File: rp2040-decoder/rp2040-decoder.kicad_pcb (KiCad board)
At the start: 4 copper layers, 19.6 x 8.6 mm, 57 parts, among them J4 5052702412, Q1 TPM2008, Q2 TPM2008, Q3 TPM2008, Q4 TPM2008, Q5 TPM2008, Q6 TPM2008, Q7 TPM2008, U1 W25Q64JVXGIQ, U2 AP63203WU, U3 RP2040, U4 MD9927, U5 MAX98357A, U6 LMV331, Y1 X252012MMB4SI

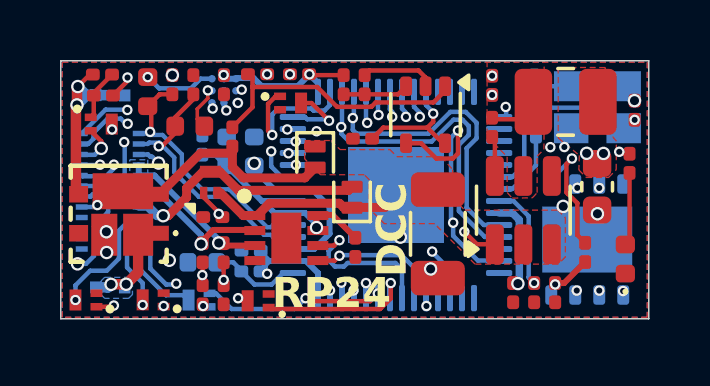
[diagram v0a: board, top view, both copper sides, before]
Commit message: fix: convert 0.2mm vias to 0.3mm
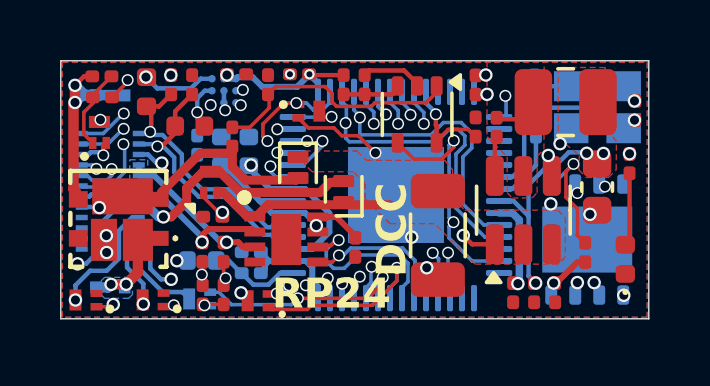
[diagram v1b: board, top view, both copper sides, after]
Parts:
- moved C5 3.79 mm to (113.8, 102.0), turned to -90 degrees
- moved D4 0.67 mm to (107.9, 103.4)
- moved Q4 0.67 mm to (108.2, 101.5)
- moved C17 0.55 mm to (113.8, 100.6)
- moved C21 0.55 mm to (105.8, 100.2), turned to 0 degrees
- moved R4 0.49 mm to (106.9, 100.6), turned to 90 degrees
- moved D3 0.34 mm to (109.4, 104.2)
- moved Q1 0.29 mm to (101.2, 102.2), turned to 90 degrees
- moved U6 0.28 mm to (111.8, 101.6)
- moved C10 0.18 mm to (105.3, 102.8)
- moved C8 0.18 mm to (106.2, 102.8)
- moved C12 0.17 mm to (104.5, 102.6)
- moved D1 0.17 mm to (101.9, 105.1)
- moved C6 0.15 mm to (114.5, 102.0)
- moved R2 0.07 mm to (101.3, 101.0)
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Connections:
- U5 pad B2: unconnected-(U5-GAIN_SLOT-PadB2) -> GND
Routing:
- net GND: track 5.86 -> 10.1 mm, vias 20 -> 21
- net Net-(U1-IO3): track 11.8 -> 15.9 mm
- net /AUX10: track 13.5 -> 11.7 mm, vias 2 -> 3
- net Net-(U1-IO2): track 19.4 -> 18.2 mm
- net +3.3V: track 43.7 -> 42.5 mm
- net Net-(Q1-G): track 1.63 -> 2.64 mm
- net /BOOT: track 15.8 -> 14.8 mm
- net /AUX3: track 14.2 -> 15.2 mm
- net /GPIO25: track 6.28 -> 7.19 mm
- net /I2S_LRCLK: track 7.67 -> 8.57 mm
- net /AUX4: track 16.6 -> 17.3 mm
- net /I2S_DIN: track 7.52 -> 8.27 mm
- net +1V1: track 20.5 -> 19.7 mm
- net /GPIO27: track 7.28 -> 8.02 mm
- net VDC: track 7.44 -> 6.84 mm
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
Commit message: fix: reduce unique part count
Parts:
- R16: value 20K -> 4.7K
- R17: value 33K -> 6.8K
- R3: value 100K -> 6.8K
- R4: value 33K -> 2.2K
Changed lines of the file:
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@@
 			)
 		)
-		(property "Value" "20K"
+		(property "Value" "4.7K"
 			(at 0 1.05 90)
 			(layer "F.Fab")
@@
 			)
 		)
-		(property "LCSC" "C473466"
+		(property "LCSC" "C270346"
 			(at 0 0 -90)
 			(unlocked yes)
@@
 			)
 		)
-		(property "Value" "100K"
+		(property "Value" "6.8K"
 			(at 0 1.05 90)
 			(layer "F.Fab")
@@
 			)
 		)
-		(property "LCSC" "C270364"
+		(property "LCSC" "C423451"
 			(at 0 0 90)
 			(unlocked yes)
@@
 			)
 		)
-		(property "Value" "33K"
+		(property "Value" "2.2K"
 			(at 0 1.05 90)
 			(layer "F.Fab")
@@
 			)
 		)
-		(property "Value" "33K"
+		(property "Value" "6.8K"
 			(at 0 1.05 90)
 			(layer "F.Fab")
@@
 			)
 		)
-		(property "LCSC" "C473534"
+		(property "LCSC" "C423451"
 			(at 0 0 90)
 			(unlocked yes)
@@
 		(tags "capacitor")
 		(property "Reference" "C21"
-			(at 0 -1.05 360)
+			(at 0 -1.05 0)
 			(layer "F.SilkS")
 			(hide yes)
@@
 		)
 		(property "Value" "100nF"
-			(at 0 1.05 360)
+			(at 0 1.05 0)
 			(layer "F.Fab")
 			(hide yes)
@@
 		)
 		(fp_text user "${REFERENCE}"
-			(at 0 -0.68 360)
+			(at 0 -0.68 0)
 			(layer "F.Fab")
 			(effects
@@
 		(tags "resistor")
 		(property "Reference" "R2"
-			(at 0 -1.05 360)
+			(at 0 -1.05 0)
 			(layer "F.SilkS")
 			(hide yes)
@@
 		)
 		(property "Value" "6.8K"
-			(at 0 1.05 360)
+			(at 0 1.05 0)
 			(layer "F.Fab")
 			(hide yes)
@@
 		)
 		(fp_text user "${REFERENCE}"
-			(at 0 -0.68 360)
+			(at 0 -0.68 0)
 			(layer "F.Fab")
 			(effects
@@
 			(at 0 0 180)
 			(unlocked yes)
+			(layer "B.Fab")
+			(hide yes)
+			(effects
+				(font
+					(size 1 1)
+					(thickness 0.15)
+				)
+				(justify mirror)
+			)
+		)
+		(property "JLCPCB_CORRECTION" "0;0;180"
+			(at 0 0 180)
+			(unlocked yes)
